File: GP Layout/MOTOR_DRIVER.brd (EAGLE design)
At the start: 91.4 x 97.5 mm, 34 parts, among them U2 CSD18502KCS_KCS_3, U3 MIC4604YM, U4 CSD18502KCS_KCS_3, U5 CSD18502KCS_KCS_3, U6 MIC4604YM, U7 ATMEGA328P_TQFP, Y1 16MHz

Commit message: Changed to two schematic sheets
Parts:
- removed C10, C11, C7, C9: (no value), resistor:153CLV-1010
- removed C8: 10uF, resistor:C050-025X075
- removed LSP4, LSP5: SE14, solpad:SE14
- removed S1: SWS006, smd-special:SMS-006
- removed SV1, SV2, SV4, SV5, SV6: (no value), con-lsta:FE10
- removed SV3: (no value), con-lsta:FE10-2
- removed U$3: LM1086IT-5.0/NOPB, TI1086:T03B
- added C12: 10uF, resistor:C050-025X075
- added C13, C14, C15, C16: (no value), resistor:153CLV-1010
- added LSP1, LSP2: SE14, solpad:SE14
- added S2: SWS006, smd-special:SMS-006
- added SV10, SV11, SV7, SV8, SV9: (no value), con-lsta:FE10
- added SV12: (no value), con-lsta:FE10-2
- added U$2: LM1086IT-5.0/NOPB, TI1086:T03B
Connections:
- removed net N$14: C10.-, C11.+
- removed net N$17: C10.+, C9.-
- removed net N$19: C7.-, C9.+
- removed net N$20: SV3.4
- removed net N$33: SV4.10
- removed net N$34: SV4.9
- removed net N$35: SV4.8
- removed net N$36: SV4.7
- removed net N$37: SV4.6
- removed net N$38: SV4.5
- removed net N$39: SV4.4
- removed net N$40: SV4.3
- removed net N$41: SV4.2
- removed net N$42: SV4.1
- new net N$21: C15.-, C16.+
- new net N$22: C14.-, C15.+
- new net N$23: C13.-, C14.+
- new net N$25: SV9.10
- new net N$26: SV9.9
- new net N$27: SV9.8
- new net N$28: SV9.7
- new net N$29: SV9.6
- new net N$30: SV9.5
- new net N$31: SV9.4
- new net N$32: SV9.3
- new net N$43: SV9.2
- new net N$44: SV9.1
- new net N$45: SV12.4
- net 3_3V: now also SV12.9; no longer SV3.9
- net 5V: now also C12.1, S2.7, SV12.18, SV12.7, U$2.2; no longer C8.1, S1.7, SV3.18, SV3.7, U$3.2
- net 5V_TEENSY: now also S2.6; no longer S1.6
- net 7_4V: now also SV7.1, U$2.3; no longer SV1.1, U$3.3
- net 7_4V_TOP: now also LSP1.MP, SV10.1; no longer LSP4.MP, SV5.1
- net BLT_RX: now also SV12.1; no longer SV3.1
- net BLT_TX: now also SV12.3; no longer SV3.3
- net CAMERA_A0: now also SV12.17; no longer SV3.17
- net CAMERA_CLK: now also SV12.13; no longer SV3.13
- net CAMERA_SI: now also SV12.15; no longer SV3.15
- net GND: now also C12.2, S2.10, S2.11, S2.12, S2.8, S2.9, SV12.11, SV12.12, SV12.14, SV12.5, U$2.1; no longer C8.2, S1.10, S1.11, S1.12, S1.8, S1.9, SV3.11, SV3.12, SV3.14, SV3.5, U$3.1
- net GND_TOP: now also C16.-, LSP2.MP, SV10.10; no longer C11.-, LSP5.MP, SV5.10
- net HALL: now also SV12.16; no longer SV3.16
- net HI: now also SV8.1; no longer SV2.1
- net HI_TOP: now also SV11.1; no longer SV6.1
- net LI: now also SV8.2; no longer SV2.2
- net LI_TOP: now also SV11.2; no longer SV6.2
- net RX: now also SV12.20; no longer SV3.20
- net SW1: now also S2.1; no longer S1.1
- net SW2: now also S2.2; no longer S1.2
- net SW3: now also S2.3; no longer S1.3
- net SW4: now also S2.4; no longer S1.4
- net SW5: now also S2.5; no longer S1.5
- net TX: now also SV12.19; no longer SV3.19

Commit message: Actual 4 schematic sheet update
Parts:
- removed C12: 10uF, resistor:C050-025X075
- removed C13, C14, C15, C16: (no value), resistor:153CLV-1010
- removed LSP1, LSP2: SE14, solpad:SE14
- removed S2: SWS006, smd-special:SMS-006
- removed SV10, SV11, SV7, SV8, SV9: (no value), con-lsta:FE10
- removed SV12: (no value), con-lsta:FE10-2
- removed U$2: LM1086IT-5.0/NOPB, TI1086:T03B
- added C10, C11, C7, C9: (no value), resistor:153CLV-1010
- added C8: 10uF, resistor:C050-025X075
- added LSP4, LSP5: SE14, solpad:SE14
- added S1: SWS006, smd-special:SMS-006
- added SV1, SV2, SV4, SV5, SV6: (no value), con-lsta:FE10
- added SV3: (no value), con-lsta:FE10-2
- added U$3: LM1086IT-5.0/NOPB, TI1086:T03B
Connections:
- removed net N$21: C15.-, C16.+
- removed net N$22: C14.-, C15.+
- removed net N$23: C13.-, C14.+
- removed net N$25: SV9.10
- removed net N$26: SV9.9
- removed net N$27: SV9.8
- removed net N$28: SV9.7
- removed net N$29: SV9.6
- removed net N$30: SV9.5
- removed net N$31: SV9.4
- removed net N$32: SV9.3
- removed net N$43: SV9.2
- removed net N$44: SV9.1
- removed net N$45: SV12.4
- new net N$14: C10.-, C11.+
- new net N$17: C10.+, C9.-
- new net N$19: C7.-, C9.+
- new net N$20: SV3.4
- new net N$33: SV4.10
- new net N$34: SV4.9
- new net N$35: SV4.8
- new net N$36: SV4.7
- new net N$37: SV4.6
- new net N$38: SV4.5
- new net N$39: SV4.4
- new net N$40: SV4.3
- new net N$41: SV4.2
- new net N$42: SV4.1
- net 3_3V: now also SV3.9; no longer SV12.9
- net 5V: now also C8.1, S1.7, SV3.18, SV3.6, SV3.7, U$3.2; no longer C12.1, S2.7, SV12.18, SV12.7, U$2.2
- net 5V_TEENSY: now also S1.6; no longer S2.6
- net 7_4V: now also SV1.1, U$3.3; no longer SV7.1, U$2.3
- net 7_4V_TOP: now also LSP4.MP, SV5.1; no longer LSP1.MP, SV10.1
- net BLT_RX: now also SV3.1; no longer SV12.1
- net BLT_TX: now also SV3.3; no longer SV12.3
- net CAMERA_A0: now also SV3.17; no longer SV12.17
- net CAMERA_CLK: now also SV3.13; no longer SV12.13
- net CAMERA_SI: now also SV3.15; no longer SV12.15
- net GND: now also C8.2, S1.10, S1.11, S1.12, S1.8, S1.9, SV3.11, SV3.12, SV3.14, SV3.2, SV3.5, U$3.1; no longer C12.2, S2.10, S2.11, S2.12, S2.8, S2.9, SV12.11, SV12.12, SV12.14, SV12.5, U$2.1
- net GND_TOP: now also C11.-, LSP5.MP, SV5.10; no longer C16.-, LSP2.MP, SV10.10
- net HALL: now also SV3.16; no longer SV12.16
- net HI: now also SV2.1; no longer SV8.1
- net HI_TOP: now also SV6.1; no longer SV11.1
- net LI: now also SV2.2; no longer SV8.2
- net LI_TOP: now also SV6.2; no longer SV11.2
- net REC_MOTOR: now also SV3.8
- net REC_SERVO: now also SV3.10
- net RX: now also SV3.20; no longer SV12.20
- net SW1: now also S1.1; no longer S2.1
- net SW2: now also S1.2; no longer S2.2
- net SW3: now also S1.3; no longer S2.3
- net SW4: now also S1.4; no longer S2.4
- net SW5: now also S1.5; no longer S2.5
- net TX: now also SV3.19; no longer SV12.19

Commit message: modified power schematic, added battery sense, named motor terminals
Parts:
- removed C10, C11, C7, C9: (no value), resistor:153CLV-1010
- added BIG_SWITCH: (no value), bigswitch:BIGSWITCH
- added C12, C13, C14, C15: (no value), resistor:153CLV-1010
- added FUSE: (no value), minifuse:FUSEHOLDER3588
- added R1: 2.8M, SparkFun-Resistors:0805
- added R2: 1.62M, SparkFun-Resistors:0805
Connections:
- net N$1 renamed MOTOR_HIGH
- net N$8 renamed MOTOR_LOW
- removed net N$14: C10.-, C11.+
- removed net N$17: C10.+, C9.-
- removed net N$19: C7.-, C9.+
- new net BATT_VOLTAGE: FUSE.A, FUSE.C, LSP4.MP, R1.2
- new net BATT_VOLTAGE_SENSE: R1.1, R2.2, U$1.14/A0
- new net N$21: BIG_SWITCH.VCC, C12.+, C13.+, C14.+, C15.+, FUSE.B, FUSE.D
- net 7_4V_TOP: now also BIG_SWITCH.GND; no longer LSP4.MP
- net GND: now also R2.1
- net GND_TOP: now also C12.-, C13.-, C14.-, C15.-; no longer C11.-

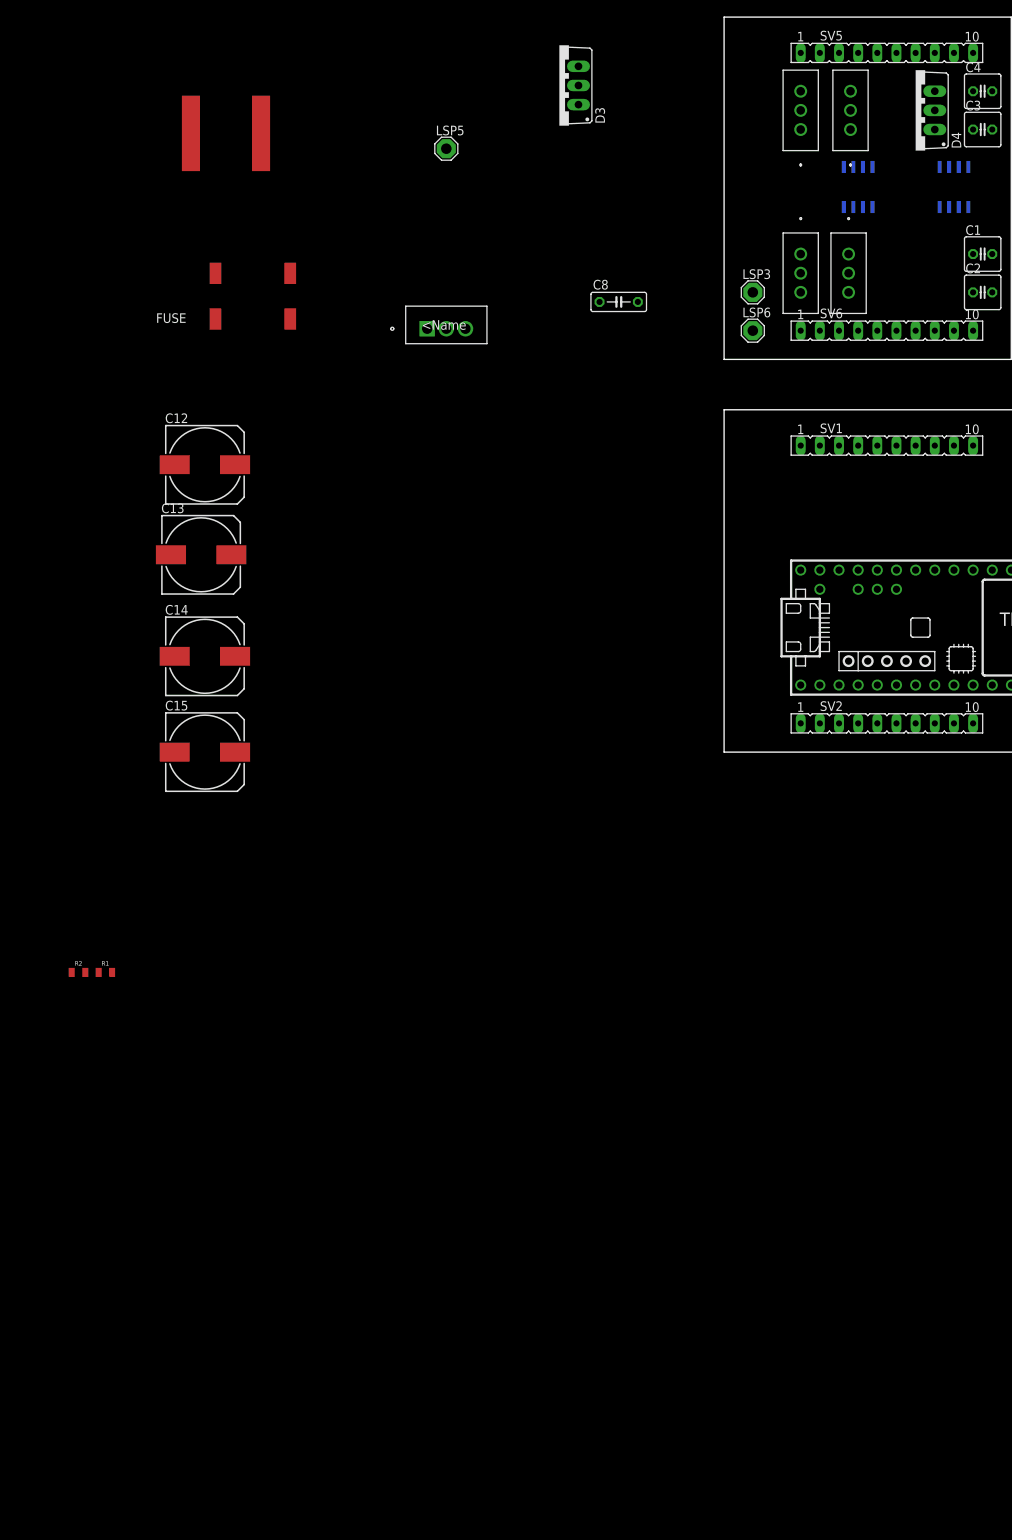
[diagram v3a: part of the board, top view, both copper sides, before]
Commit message: added some heatsink outlines
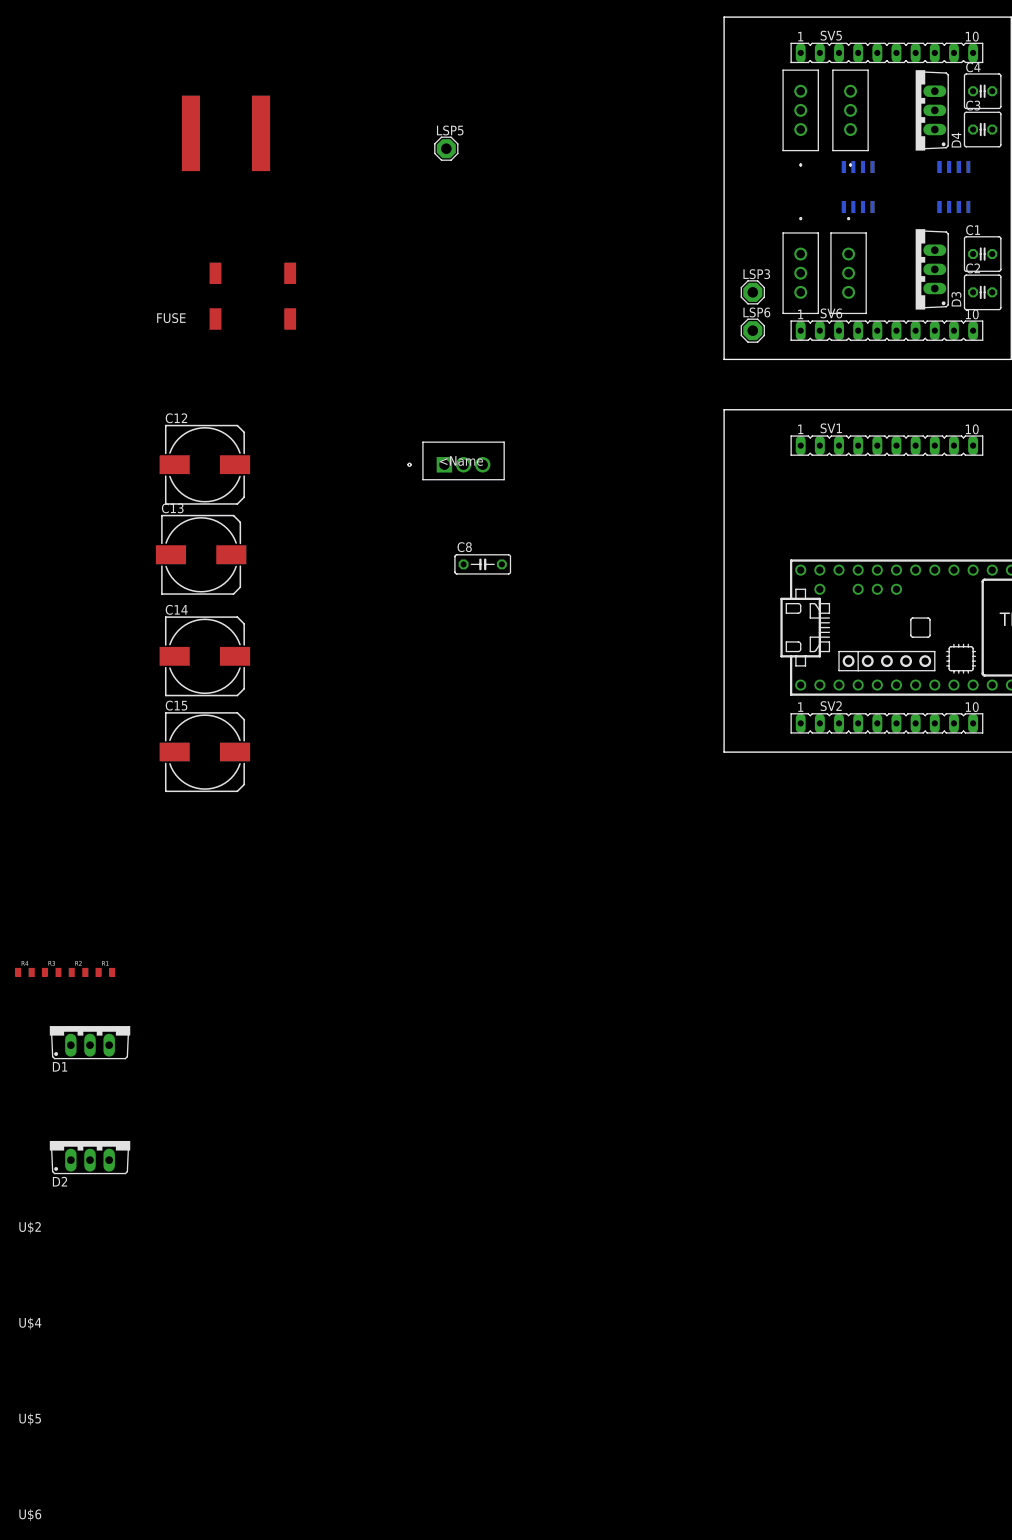
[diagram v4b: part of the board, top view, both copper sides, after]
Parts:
- added D1, D2: BYV32, diode:TO220ABS
- added R3: 2.32M, SparkFun-Resistors:0805
- added R4: 1.15M, SparkFun-Resistors:0805
- added U$2, U$4, U$5, U$6: HEATSINK, heatsink:HEATSINK
- moved D3 53.2 mm to (25.4, 64.0)
- moved C8 39.2 mm to (-32.0, 24.9)
- moved U$3 18.2 mm to (-32.0, 39.1)
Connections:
- new net EMF_SENSE_HIGH: D1.C, U$1.17/A3
- new net EMF_SENSE_LOW: D2.C, U$1.16/A2
- new net MOTOR_HIGH_TOP: LSP3.MP, SV6.3, TOP_FWD.3, U2.2
- new net MOTOR_LOW_TOP: LSP6.MP, SV6.4, U4.3, U5.2
- new net N$1: D1.A1, D1.A2, R3.1, R4.2
- net 5V: no longer U7.18, U7.29, U7.4, U7.6
- net 5V_TEENSY: now also U7.18, U7.29, U7.4, U7.6
- net MOTOR_HIGH: now also R3.2, SV2.3; no longer LSP3.MP, TOP_FWD.3, U2.2
- net MOTOR_LOW: now also D2.A1, D2.A2, R4.1, SV2.4; no longer LSP6.MP, U4.3, U5.2
